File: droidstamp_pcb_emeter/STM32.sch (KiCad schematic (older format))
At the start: 32 parts, among them P6 CONN_13X2, P8 CONN_12X2, P9 CONN_12X2, U11 LT1117CST-3.3, U9 STM32F4_LQFP100, X3 12MHz

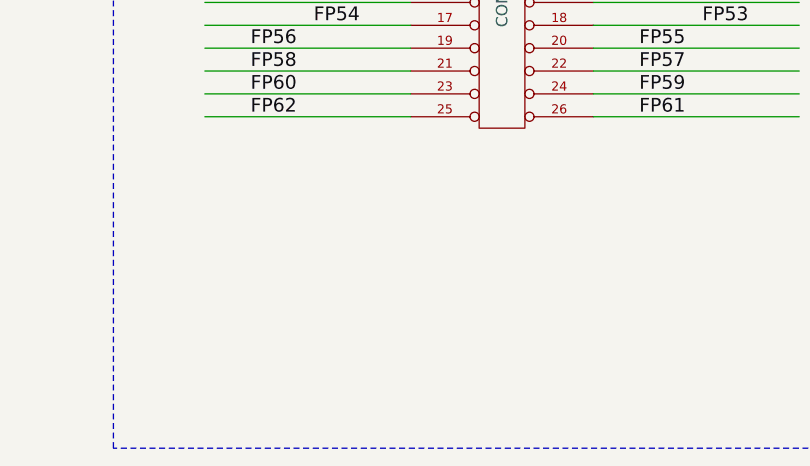
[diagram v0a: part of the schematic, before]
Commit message: Fixed some routing and PCB paths
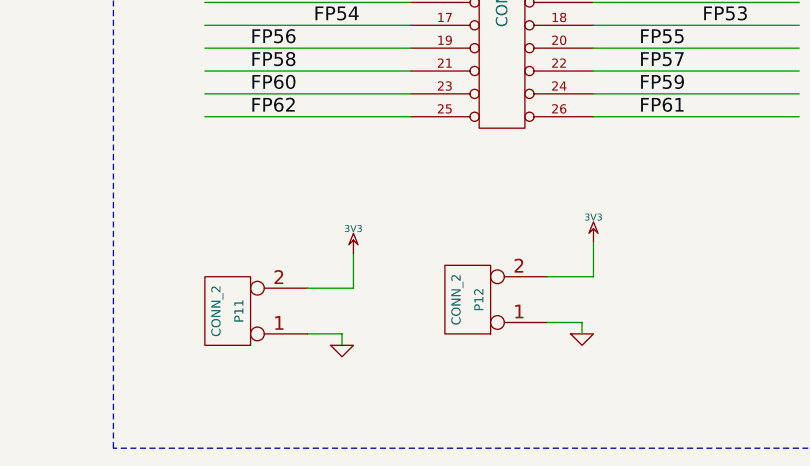
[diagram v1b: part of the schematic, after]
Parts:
- added P11, P12: CONN_2, symbol CONN_2
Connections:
- wire segments 243 -> 251
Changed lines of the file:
@@
-EESchema Schematic File Version 2  date jue 19 abr 2012 22:22:20 COT
+EESchema Schematic File Version 2  date vie 20 abr 2012 12:34:33 COT
 LIBS:con-jack
 LIBS:zxct1009
@@
 Comment4 ""
 $EndDescr
-Text Label 5950 2500 0    60   ~ 0
-VREF
+$Comp
+L CONN_2 P12
+U 1 1 4F9177EF
+P 14150 9750
+F 0 "P12" V 14100 9750 40  0000 C CNN
+F 1 "CONN_2" V 14200 9750 40  0000 C CNN
+	1    14150 9750
+	-1   0    0    1
+$EndComp
+$Comp
+L GND #PWR0100
+U 1 1 4F9177EE
+P 14650 9900
+F 0 "#PWR0100" H 14650 9900 30  0001 C CNN
+F 1 "GND" H 14650 9830 30  0001 C CNN
+	1    14650 9900
+	1    0    0    -1
+$EndComp
+$Comp
+L 3V3 #PWR0101
+U 1 1 4F9177ED
+P 14700 9500
+F 0 "#PWR0101" H 14700 9600 30  0001 C CNN
+F 1 "3V3" H 14700 9610 30  0000 C CNN
+	1    14700 9500
+	1    0    0    -1
+$EndComp
+Wire Wire Line
+	14650 9900 14650 9850
+Wire Wire Line
+	14650 9850 14500 9850
+Wire Wire Line
+	14500 9650 14700 9650
+Wire Wire Line
+	14700 9650 14700 9500
+$Comp
+L CONN_13X2 P6
+U 1 1 4F9054FB
+P 14300 8350
+F 0 "P6" H 14300 9050 60  0000 C CNN
+F 1 "CONN_13X2" V 14300 8350 50  0000 C CNN
+	1    14300 8350
+	1    0    0    -1
+$EndComp
+Wire Wire Line
+	13650 9550 13650 9700
+Wire Wire Line
+	13650 9700 13450 9700
 Connection ~ 14000 5550
 Wire Wire Line
@@
 Wire Wire Line
 	14000 5500 14000 5600
-$Comp
-L GND #PWR0100
+Wire Wire Line
+	13450 9900 13600 9900
+Wire Wire Line
+	13600 9900 13600 9950
+$Comp
+L 3V3 #PWR0102
+U 1 1 4F9176B1
+P 13650 9550
+F 0 "#PWR0102" H 13650 9650 30  0001 C CNN
+F 1 "3V3" H 13650 9660 30  0000 C CNN
+	1    13650 9550
+	1    0    0    -1
+$EndComp
+$Comp
+L GND #PWR0103
+U 1 1 4F9176A5
+P 13600 9950
+F 0 "#PWR0103" H 13600 9950 30  0001 C CNN
+F 1 "GND" H 13600 9880 30  0001 C CNN
+	1    13600 9950
+	1    0    0    -1
+$EndComp
+$Comp
+L CONN_2 P11
+U 1 1 4F917692
+P 13100 9800
+F 0 "P11" V 13050 9800 40  0000 C CNN
+F 1 "CONN_2" V 13150 9800 40  0000 C CNN
+	1    13100 9800
+	-1   0    0    1
+$EndComp
+$Comp
+L CONN_12X2 P9
+U 1 1 4E831B93
+P 14450 6550
+F 0 "P9" H 14450 7200 60  0000 C CNN
+F 1 "CONN_12X2" V 14450 6550 50  0000 C CNN
+F 2 "pin_array_12x2" H 14450 6550 60  0001 C CNN
+	1    14450 6550
+	1    0    0    -1
+$EndComp
+Text Label 5950 2500 0    60   ~ 0
+VREF
+$Comp
+L GND #PWR0104
 U 1 1 4F90D1B0
 P 13550 5700
-F 0 "#PWR0100" H 13550 5700 30  0001 C CNN
+F 0 "#PWR0104" H 13550 5700 30  0001 C CNN
 F 1 "GND" H 13550 5630 30  0001 C CNN
 	1    13550 5700
@@
 $EndComp
 $Comp
-L GND #PWR0101
+L GND #PWR0105
 U 1 1 4F90D1AD
 P 15350 5650
-F 0 "#PWR0101" H 15350 5650 30  0001 C CNN
+F 0 "#PWR0105" H 15350 5650 30  0001 C CNN
 F 1 "GND" H 15350 5580 30  0001 C CNN
 	1    15350 5650
@@
 NoConn ~ 6750 6000
 NoConn ~ 6750 5900
-$Comp
-L CONN_13X2 P6
-U 1 1 4F9054FB
-P 14300 8350
-F 0 "P6" H 14300 9050 60  0000 C CNN
-F 1 "CONN_13X2" V 14300 8350 50  0000 C CNN
-	1    14300 8350
-	1    0    0    -1
-$EndComp
 Text Label 1050 5200 0    60   ~ 0
 FP67
@@
 FP52
 $Comp
-L GND #PWR0102
+L GND #PWR0106
 U 1 1 4F8F84A2
 P 1600 2550
-F 0 "#PWR0102" H 1600 2550 30  0001 C CNN
+F 0 "#PWR0106" H 1600 2550 30  0001 C CNN
 F 1 "GND" H 1600 2480 30  0001 C CNN
 	1    1600 2550
@@
 $EndComp
 $Comp
-L 3V3 #PWR0103
+L 3V3 #PWR0107
 U 1 1 4F8F849B
 P 1600 2150
-F 0 "#PWR0103" H 1600 2250 30  0001 C CNN
+F 0 "#PWR0107" H 1600 2250 30  0001 C CNN
 F 1 "3V3" H 1600 2260 30  0000 C CNN
 	1    1600 2150
@@
 VCAP_1
 $Comp
-L 3V3 #PWR0104
+L 3V3 #PWR0108
 U 1 1 4F8F56B6
 P 6450 2800
-F 0 "#PWR0104" H 6450 2900 30  0001 C CNN
+F 0 "#PWR0108" H 6450 2900 30  0001 C CNN
 F 1 "3V3" H 6450 2910 30  0000 C CNN
 	1    6450 2800
@@
 $EndComp
 $Comp
-L VDD5V #PWR0105
+L VDD5V #PWR0109
 U 1 1 4F8D365D
 P 13450 2350
-F 0 "#PWR0105" H 13450 2450 30  0001 C CNN
+F 0 "#PWR0109" H 13450 2450 30  0001 C CNN
 F 1 "VDD5V" H 13450 2450 30  0000 C CNN
 	1    13450 2350
@@
 C19, C21 2.2uF para cortex M4\nC19. C21 = Ohms para cortex M3
 $Comp
-L GND #PWR0106
+L GND #PWR0110
 U 1 1 4F3EDF01
 P 4300 7900
-F 0 "#PWR0106" H 4300 7900 30  0001 C CNN
+F 0 "#PWR0110" H 4300 7900 30  0001 C CNN
 F 1 "GND" H 4300 7830 30  0001 C CNN
 	1    4300 7900
@@
 $EndComp
 $Comp
-L 3V3 #PWR0107
+L 3V3 #PWR0111
 U 1 1 4F352D37
 P 11050 6000
-F 0 "#PWR0107" H 11050 6100 30  0001 C CNN
+F 0 "#PWR0111" H 11050 6100 30  0001 C CNN
 F 1 "3V3" H 11050 6110 30  0000 C CNN
 	1    11050 6000
@@
 I2C1_SDA
 $Comp
-L 3V3 #PWR0108
+L 3V3 #PWR0112
 U 1 1 4E8A0997
 P 15500 4500
-F 0 "#PWR0108" H 15500 4600 30  0001 C CNN
+F 0 "#PWR0112" H 15500 4600 30  0001 C CNN
 F 1 "3V3" H 15500 4610 30  0000 C CNN
 	1    15500 4500
@@
 FP37
 $Comp
-L CONN_12X2 P9
-U 1 1 4E831B93
-P 14450 6550
-F 0 "P9" H 14450 7200 60  0000 C CNN
-F 1 "CONN_12X2" V 14450 6550 50  0000 C CNN
-F 2 "pin_array_12x2" H 14450 6550 60  0001 C CNN
-	1    14450 6550
-	1    0    0    -1
-$EndComp
-$Comp
-L VDD5V #PWR0109
+L VDD5V #PWR0113
 U 1 1 4E7B5061
 P 13450 2350
-F 0 "#PWR0109" H 13450 2450 30  0001 C CNN
+F 0 "#PWR0113" H 13450 2450 30  0001 C CNN
 F 1 "VDD5V" H 13450 2450 30  0000 C CNN
 	1    13450 2350
@@
 $EndComp
 $Comp
-L GND #PWR0110
+L GND #PWR0114
 U 1 1 4E7B4E89
 P 13450 3000
-F 0 "#PWR0110" H 13450 3000 30  0001 C CNN
+F 0 "#PWR0114" H 13450 3000 30  0001 C CNN
 F 1 "GND" H 13450 2930 30  0001 C CNN
 	1    13450 3000
@@
 $EndComp
 $Comp
-L GND #PWR0111
+L GND #PWR0115
 U 1 1 4E7B4E84
 P 14900 3000
-F 0 "#PWR0111" H 14900 3000 30  0001 C CNN
+F 0 "#PWR0115" H 14900 3000 30  0001 C CNN
 F 1 "GND" H 14900 2930 30  0001 C CNN
 	1    14900 3000
@@
 $EndComp
 $Comp
-L GND #PWR0112
+L GND #PWR0116
 U 1 1 4E7B44BE
 P 14500 3000
-F 0 "#PWR0112" H 14500 3000 30  0001 C CNN
+F 0 "#PWR0116" H 14500 3000 30  0001 C CNN
 F 1 "GND" H 14500 2930 30  0001 C CNN
 	1    14500 3000
@@
 $EndComp
 $Comp
-L GND #PWR0113
+L GND #PWR0117
 U 1 1 4E7B44A2
 P 13650 2600
-F 0 "#PWR0113" H 13650 2600 30  0001 C CNN
+F 0 "#PWR0117" H 13650 2600 30  0001 C CNN
 F 1 "GND" H 13650 2530 30  0001 C CNN
 	1    13650 2600
@@
 $EndComp
 $Comp
-L 3V3 #PWR0114
+L 3V3 #PWR0118
 U 1 1 4E7B4482
 P 14900 2250
-F 0 "#PWR0114" H 14900 2350 30  0001 C CNN
+F 0 "#PWR0118" H 14900 2350 30  0001 C CNN
 F 1 "3V3" H 14900 2360 30  0000 C CNN
 	1    14900 2250
@@
 $EndComp
 $Comp
-L GND #PWR0115
+L GND #PWR0119
 U 1 1 4E78C5F4
 P 11000 5600
-F 0 "#PWR0115" H 11000 5600 30  0001 C CNN
+F 0 "#PWR0119" H 11000 5600 30  0001 C CNN
 F 1 "GND" H 11000 5530 30  0001 C CNN
 	1    11000 5600
@@
 $EndComp
 $Comp
-L 3V3 #PWR0116
+L 3V3 #PWR0120
 U 1 1 4E78C319
 P 11500 2250
-F 0 "#PWR0116" H 11500 2350 30  0001 C CNN
+F 0 "#PWR0120" H 11500 2350 30  0001 C CNN
 F 1 "3V3" H 11500 2360 30  0000 C CNN
 	1    11500 2250
@@
 $EndComp
 $Comp
-L GND #PWR0117
+L GND #PWR0121
 U 1 1 4E78C2ED
 P 5300 7850
-F 0 "#PWR0117" H 5300 7850 30  0001 C CNN
+F 0 "#PWR0121" H 5300 7850 30  0001 C CNN
 F 1 "GND" H 5300 7780 30  0001 C CNN
 	1    5300 7850
@@
 JTDI
 $Comp
-L 3V3 #PWR0118
+L 3V3 #PWR0122
 U 1 1 4E78BA06
 P 4300 1900
-F 0 "#PWR0118" H 4300 2000 30  0001 C CNN
+F 0 "#PWR0122" H 4300 2000 30  0001 C CNN
 F 1 "3V3" H 4300 2010 30  0000 C CNN
 	1    4300 1900
@@
 $EndComp
 $Comp
-L 3V3 #PWR0119
+L 3V3 #PWR0123
 U 1 1 4E2A2E11
 P 11450 1050
-F 0 "#PWR0119" H 11450 1150 30  0001 C CNN
+F 0 "#PWR0123" H 11450 1150 30  0001 C CNN
 F 1 "3V3" H 11450 1160 30  0000 C CNN
 	1    11450 1050
@@
 $EndComp
 $Comp
-L 3V3 #PWR0120
+L 3V3 #PWR0124
 U 1 1 4E2A2E03
 P 13150 1300
-F 0 "#PWR0120" H 13150 1400 30  0001 C CNN
+F 0 "#PWR0124" H 13150 1400 30  0001 C CNN
 F 1 "3V3" H 13150 1410 30  0000 C CNN
 	1    13150 1300
@@
 $EndComp
 $Comp
-L GND #PWR0121
+L GND #PWR0125
 U 1 1 4E188E4E
 P 14950 1800
-F 0 "#PWR0121" H 14950 1800 30  0001 C CNN
+F 0 "#PWR0125" H 14950 1800 30  0001 C CNN
 F 1 "GND" H 14950 1730 30  0001 C CNN
 	1    14950 1800
@@
 FP14
 $Comp
-L GND #PWR0122
+L GND #PWR0126
 U 1 1 4E186DEB
 P 13650 1800
-F 0 "#PWR0122" H 13650 1800 30  0001 C CNN
+F 0 "#PWR0126" H 13650 1800 30  0001 C CNN
 F 1 "GND" H 13650 1730 30  0001 C CNN
 	1    13650 1800
@@
 USART2_TX
 $Comp
-L GND #PWR0123
+L GND #PWR0127
 U 1 1 4E07869F
 P 12150 1700
-F 0 "#PWR0123" H 12150 1700 30  0001 C CNN
+F 0 "#PWR0127" H 12150 1700 30  0001 C CNN
 F 1 "GND" H 12150 1630 30  0001 C CNN
 	1    12150 1700
@@
 $EndComp
 $Comp
-L GND #PWR0124
+L GND #PWR0128
 U 1 1 4DCDB183
 P 12450 2950
-F 0 "#PWR0124" H 12450 2950 30  0001 C CNN
+F 0 "#PWR0128" H 12450 2950 30  0001 C CNN
 F 1 "GND" H 12450 2880 30  0001 C CNN
 	1    12450 2950
@@
 NRST
 $Comp
-L GND #PWR0125
+L GND #PWR0129
 U 1 1 4DCDB180
 P 7850 3000
-F 0 "#PWR0125" H 7850 3000 30  0001 C CNN
+F 0 "#PWR0129" H 7850 3000 30  0001 C CNN
 F 1 "GND" H 7850 2930 30  0001 C CNN
 	1    7850 3000
@@
 BOOT0
 $Comp
-L GND #PWR0126
+L GND #PWR0130
 U 1 1 4DCDB17D
 P 10600 5600
-F 0 "#PWR0126" H 10600 5600 30  0001 C CNN
+F 0 "#PWR0130" H 10600 5600 30  0001 C CNN
 F 1 "GND" H 10600 5530 30  0001 C CNN
 	1    10600 5600

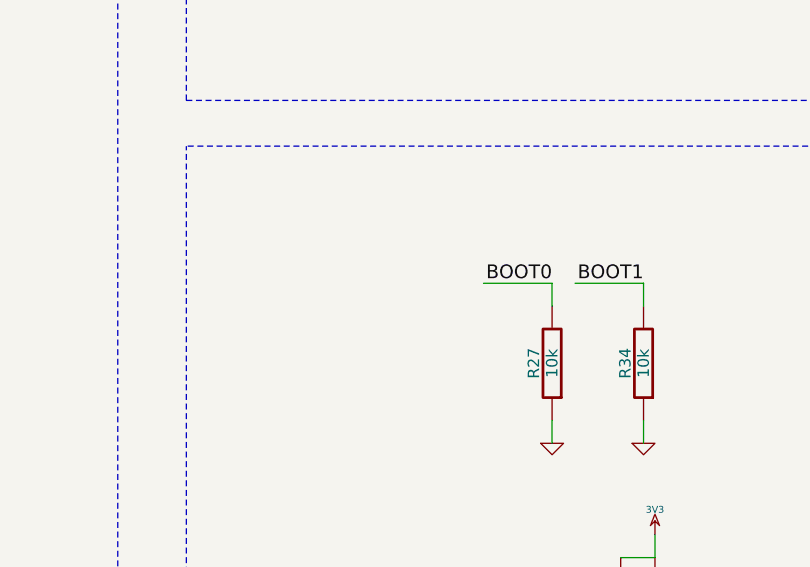
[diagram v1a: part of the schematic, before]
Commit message: Adición de la linea BOOT_MODE para modificar el inicio del stm32 desde memoria interna o jtag
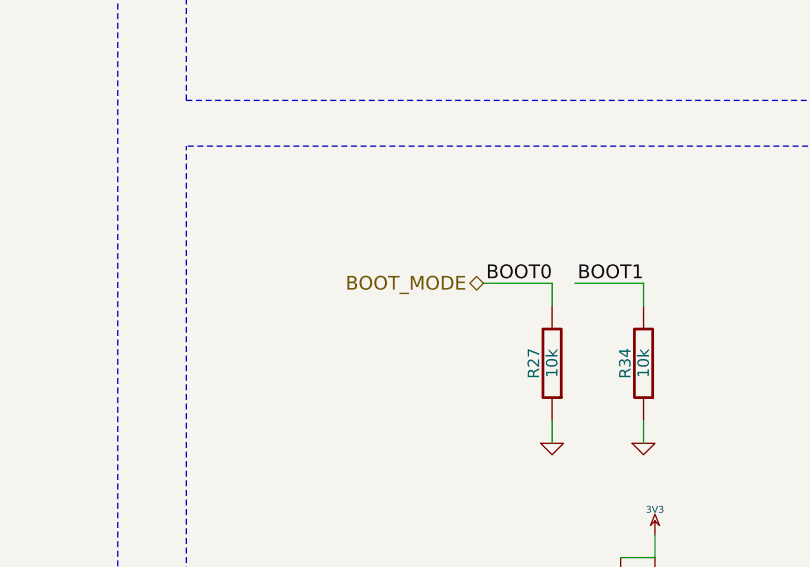
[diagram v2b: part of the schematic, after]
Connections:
- net labels added: BOOT_MODE
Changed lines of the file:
@@
-EESchema Schematic File Version 2  date vie 20 abr 2012 12:34:33 COT
+EESchema Schematic File Version 2  date Tue 21 Aug 2012 09:23:06 AM COT
 LIBS:con-jack
 LIBS:zxct1009
@@
 Sheet 4 5
 Title ""
-Date "20 apr 2012"
+Date "21 aug 2012"
 Rev ""
 Comp ""
@@
 Comment4 ""
 $EndDescr
+Text HLabel 10300 4900 0    60   BiDi ~ 0
+BOOT_MODE
 $Comp
 L CONN_2 P12
